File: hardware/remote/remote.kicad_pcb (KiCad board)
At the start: 2 copper layers, 106.7 x 86.4 mm, 25 parts

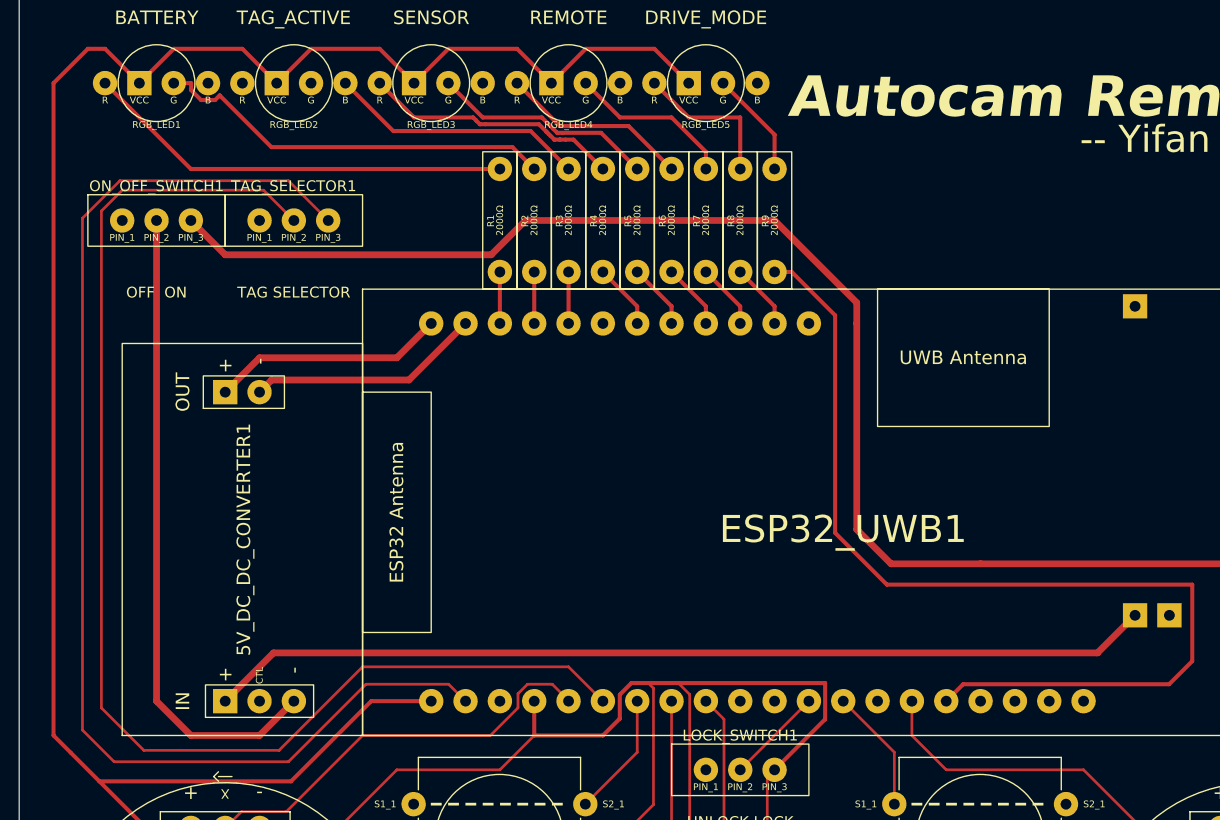
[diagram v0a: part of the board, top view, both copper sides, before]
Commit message: hardware/remote: Minor update to make more clearance for the antenna
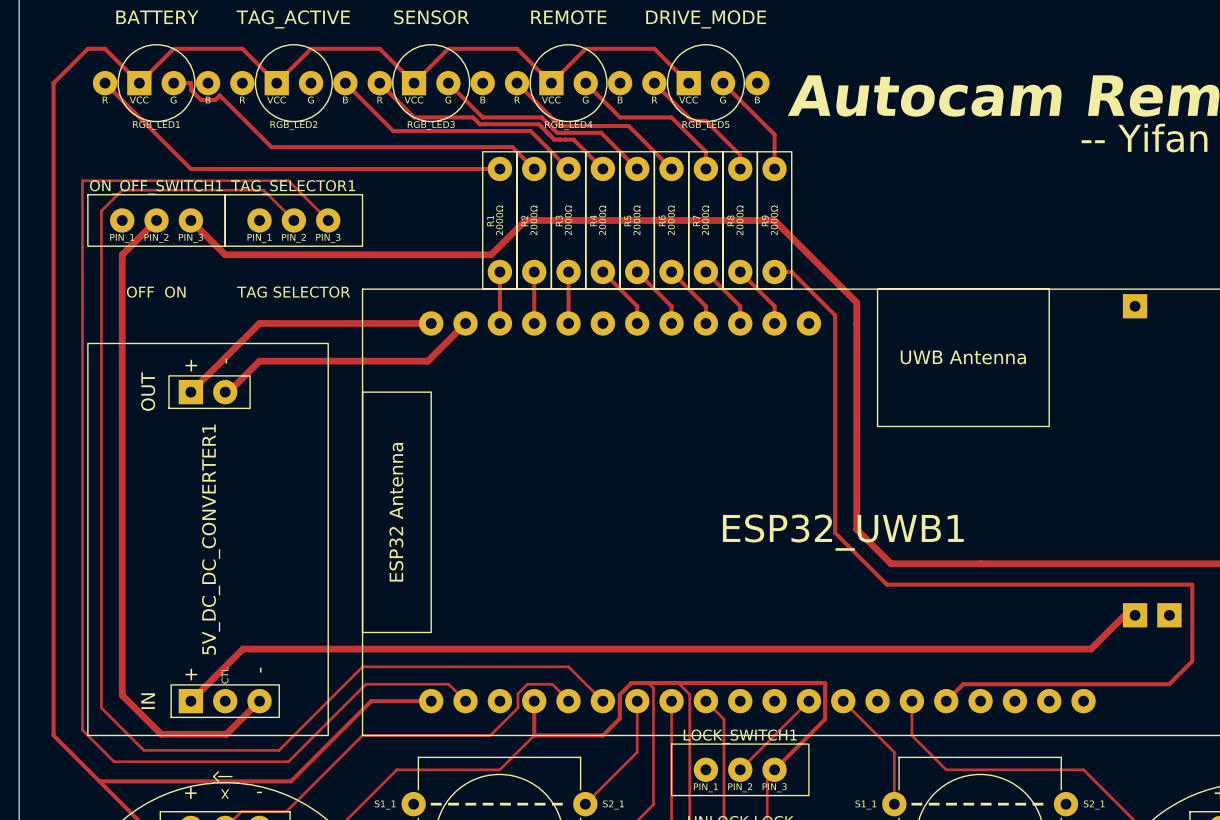
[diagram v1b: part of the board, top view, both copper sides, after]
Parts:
- moved 5V_DC_DC_CONVERTER1 2.54 mm to (99.1, 116.6)
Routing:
- net Net-(5V_DC_DC_CONVERTER1-OUT_-): track 17.3 -> 19.9 mm
- net Net-(5V_DC_DC_CONVERTER1-OUT_+): track 17.3 -> 19.9 mm
- net Net-(3.7V_BATTERY_CHARGER1-OUT+): track 69.9 -> 72.5 mm
- net Net-(RGB_LED5-R): track 11.2 -> 9.58 mm
- net Net-(ESP32_UWB1-GND-Pad2): track 90.6 -> 92.2 mm
- net Net-(5V_DC_DC_CONVERTER1-IN_-): track 47.8 -> 48.5 mm
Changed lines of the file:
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@@
 	(footprint "Autocam:5V DC-DC Step Up Converter (Rectangle)"
 		(layer "F.Cu")
-		(at 101.6 116.591058 90)
+		(at 99.06 116.591058 90)
 		(property "Reference" "5V_DC_DC_CONVERTER1"
 			(at 14.5 9 90)
@@
 	)
 	(segment
+		(start 110.531058 110.2)
+		(end 106.68 114.051058)
+		(width 0.5)
+		(layer "F.Cu")
+		(net 3)
+	)
+	(segment
 		(start 176.53 107.701058)
-		(end 173.750085 110.480973)
+		(end 175.769942 107.701058)
 		(width 0.5)
 		(layer "F.Cu")
@@
 	)
 	(segment
-		(start 112.790085 110.480973)
-		(end 109.22 114.051058)
+		(start 173.271 110.2)
+		(end 110.531058 110.2)
 		(width 0.5)
 		(layer "F.Cu")
@@
 	)
 	(segment
-		(start 173.750085 110.480973)
-		(end 112.790085 110.480973)
+		(start 175.769942 107.701058)
+		(end 173.271 110.2)
 		(width 0.5)
 		(layer "F.Cu")
@@
 	)
 	(segment
-		(start 112.66 90.291058)
-		(end 122.82 90.291058)
+		(start 124.211058 88.9)
+		(end 127 86.111058)
 		(width 0.5)
 		(layer "F.Cu")
@@
 	)
 	(segment
-		(start 122.82 90.291058)
-		(end 127 86.111058)
+		(start 109.468942 91.191058)
+		(end 111.76 88.9)
 		(width 0.5)
 		(layer "F.Cu")
@@
 	)
 	(segment
-		(start 111.76 91.191058)
-		(end 112.66 90.291058)
+		(start 109.22 91.191058)
+		(end 109.468942 91.191058)
 		(width 0.5)
 		(layer "F.Cu")
@@
 	)
 	(segment
-		(start 111.76 88.651058)
-		(end 121.92 88.651058)
+		(start 111.76 88.9)
+		(end 124.211058 88.9)
 		(width 0.5)
 		(layer "F.Cu")
-		(net 8)
+		(net 7)
 	)
 	(segment
-		(start 121.92 88.651058)
+		(start 111.76 86.111058)
 		(end 124.46 86.111058)
 		(width 0.5)
@@
 	)
 	(segment
-		(start 109.22 91.191058)
-		(end 111.76 88.651058)
+		(start 106.68 91.191058)
+		(end 111.76 86.111058)
 		(width 0.5)
 		(layer "F.Cu")
@@
 	)
 	(segment
-		(start 106.68 116.591058)
-		(end 111.76 116.591058)
+		(start 104.48 116.5)
+		(end 101.6 113.62)
 		(width 0.5)
 		(layer "F.Cu")
@@
 	)
 	(segment
-		(start 104.14 114.051058)
-		(end 106.68 116.591058)
+		(start 101.6 81.031058)
+		(end 104.14 78.491058)
 		(width 0.5)
 		(layer "F.Cu")
@@
 	)
 	(segment
-		(start 111.76 116.591058)
-		(end 114.3 114.051058)
+		(start 111.76 114.051058)
+		(end 109.311058 116.5)
 		(width 0.5)
 		(layer "F.Cu")
@@
 	)
 	(segment
-		(start 104.14 78.491058)
-		(end 104.14 114.051058)
+		(start 101.6 113.62)
+		(end 101.6 81.031058)
+		(width 0.5)
+		(layer "F.Cu")
+		(net 9)
+	)
+	(segment
+		(start 109.311058 116.5)
+		(end 104.48 116.5)
 		(width 0.5)
 		(layer "F.Cu")
@@
 	)
 	(segment
-		(start 119.631 112.800058)
-		(end 125.749 112.800058)
+		(start 98.659 116.190058)
+		(end 101.001 118.532058)
 		(width 0.2)
 		(layer "F.Cu")
@@
 	)
 	(segment
-		(start 98.659 116.190058)
-		(end 101.001 118.532058)
-		(width 0.2)
-		(layer "F.Cu")
-		(net 59)
-	)
-	(segment
-		(start 116.84 78.491058)
-		(end 113.899 75.550058)
+		(start 101.001 118.532058)
+		(end 113.899 118.532058)
 		(width 0.2)
 		(layer "F.Cu")
@@
 	)
 	(segment
-		(start 98.659 78.324958)
+		(start 98.659 75.550058)
 		(end 98.659 116.190058)
 		(width 0.2)
@@
 	)
 	(segment
-		(start 101.4339 75.550058)
-		(end 98.659 78.324958)
+		(start 113.899 75.550058)
+		(end 98.659 75.550058)
 		(width 0.2)
 		(layer "F.Cu")
@@
 	)
 	(segment
-		(start 113.899 75.550058)
-		(end 101.4339 75.550058)
+		(start 119.631 112.800058)
+		(end 125.749 112.800058)
 		(width 0.2)
 		(layer "F.Cu")
@@
 	)
 	(segment
-		(start 101.001 118.532058)
-		(end 113.899 118.532058)
+		(start 116.84 78.491058)
+		(end 113.899 75.550058)
 		(width 0.2)
 		(layer "F.Cu")
@@
 	)
 	(segment
-		(start 147.32 70.871058)
-		(end 147.32 74.681058)
+		(start 144.78 71.12)
+		(end 143.758942 71.12)
+		(width 0.3)
+		(layer "F.Cu")
+		(net 71)
+	)
+	(segment
+		(start 147.32 73.66)
+		(end 144.78 71.12)
 		(width 0.3)
 		(layer "F.Cu")
@@
 	)
 	(segment
-		(start 143.51 70.871058)
-		(end 147.32 70.871058)
+		(start 143.758942 71.12)
+		(end 140.97 68.331058)
 		(width 0.3)
 		(layer "F.Cu")
@@
 	)
 	(segment
-		(start 140.97 68.331058)
-		(end 143.51 70.871058)
+		(start 147.32 74.681058)
+		(end 147.32 73.66)
 		(width 0.3)
 		(layer "F.Cu")

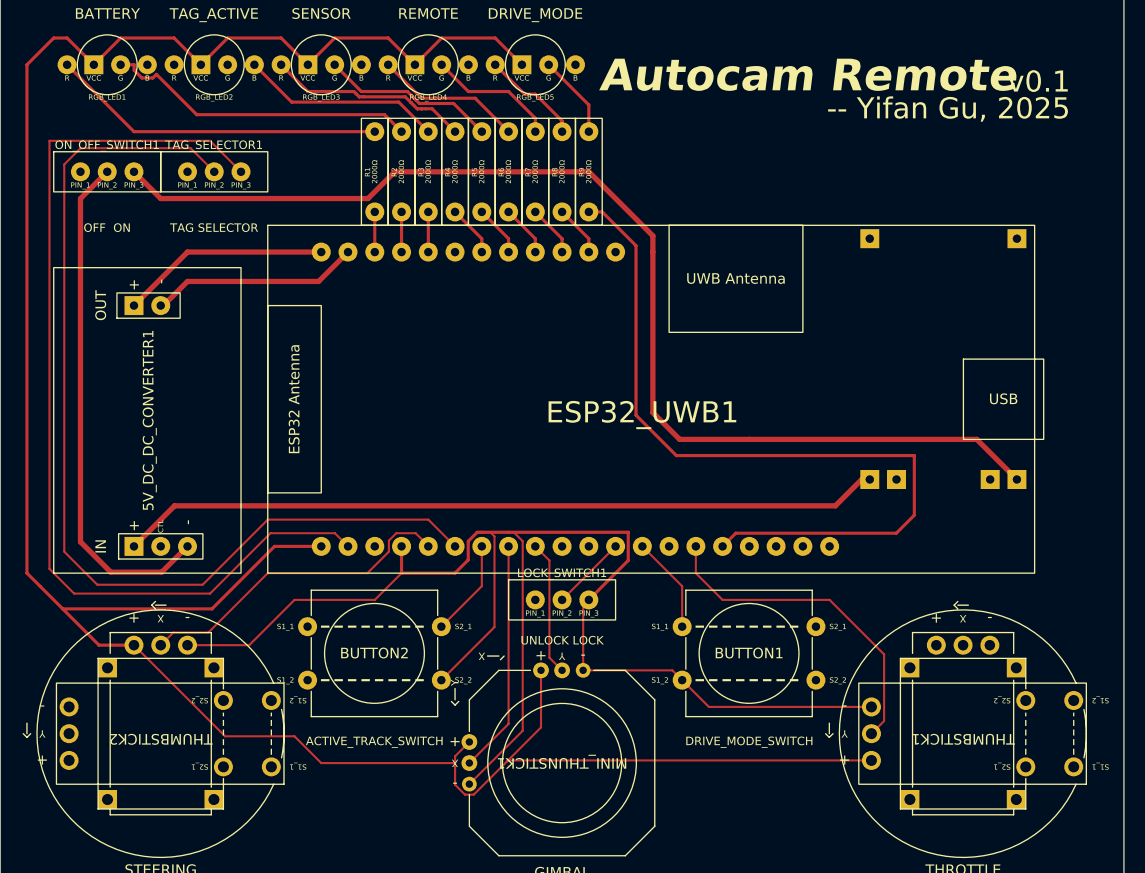
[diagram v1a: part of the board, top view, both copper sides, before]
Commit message: remote: Add battery status LED logic.
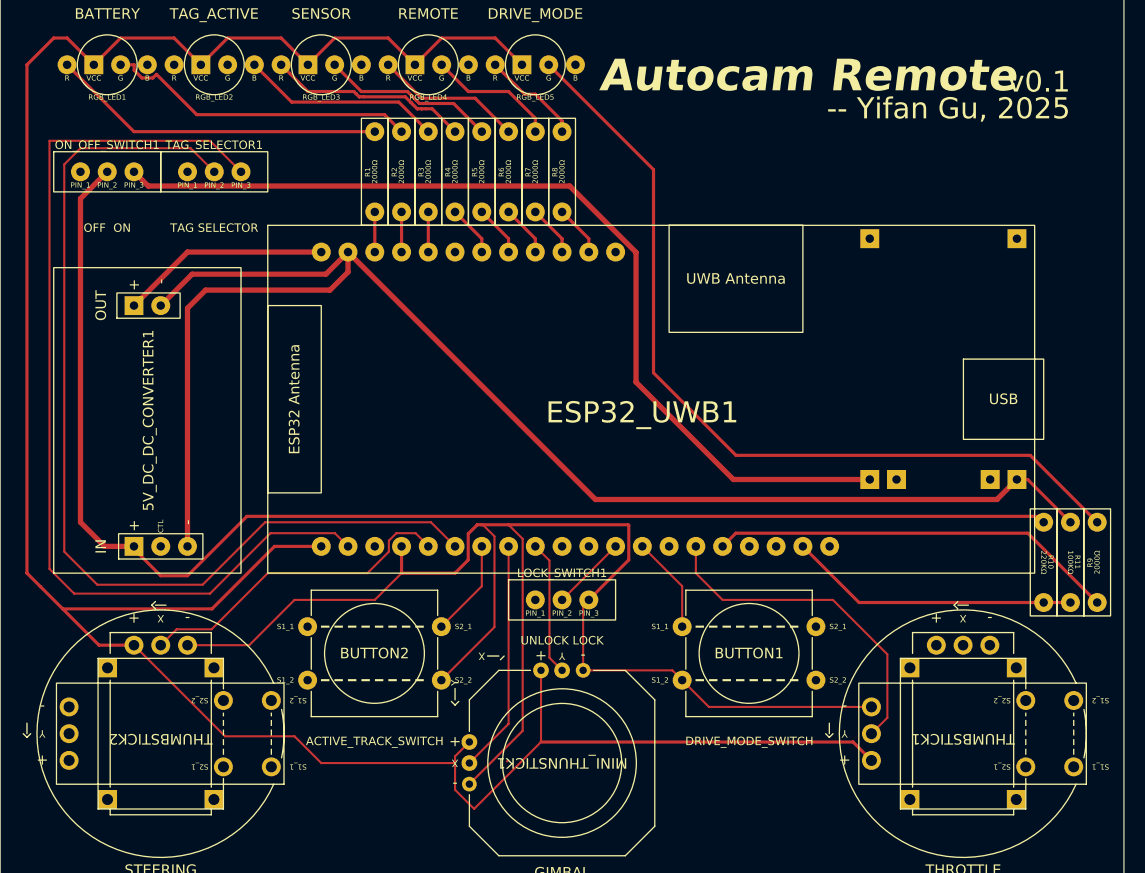
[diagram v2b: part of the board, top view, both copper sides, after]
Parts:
- added R10: 220KΩ, Autocam:Simple Resistor, F.Cu at (193.0, 111.8)
- added R11: 100KΩ, Autocam:Simple Resistor, F.Cu at (195.6, 111.8)
- moved R9 60.9 mm to (198.1, 119.4)
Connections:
- 5V_DC_DC_CONVERTER1 pad 1: Net-(3.7V_BATTERY_CHARGER1-OUT+) -> Net-(5V_DC_DC_CONVERTER1-IN_+)
- 5V_DC_DC_CONVERTER1 pad 3: Net-(5V_DC_DC_CONVERTER1-IN_-) -> Net-(3.7V_BATTERY_CHARGER1-OUT-)
- 5V_DC_DC_CONVERTER1 pad 5: Net-(5V_DC_DC_CONVERTER1-OUT_-) -> Net-(3.7V_BATTERY_CHARGER1-OUT-)
- ESP32_UWB1 pad 19: unconnected-(ESP32_UWB1-IO36-Pad19) -> Net-(ESP32_UWB1-IO36)
- ESP32_UWB1 pad 22: Net-(5V_DC_DC_CONVERTER1-OUT_-) -> Net-(3.7V_BATTERY_CHARGER1-OUT-)
- ON_OFF_SWITCH1 pad 2: Net-(5V_DC_DC_CONVERTER1-IN_-) -> Net-(5V_DC_DC_CONVERTER1-IN_+)
- ON_OFF_SWITCH1 pad 3: Net-(3.7V_BATTERY_CHARGER1-OUT-) -> Net-(3.7V_BATTERY_CHARGER1-OUT+)
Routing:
- net Net-(5V_DC_DC_CONVERTER1-IN_+): track 0.00 -> 129.8 mm
- net Net-(RGB_LED5-G): track 7.93 -> 81.4 mm
- net Net-(5V_DC_DC_CONVERTER1-IN_-): track 48.5 -> 0.00 mm
- net Net-(ESP32_UWB1-IO33): track 75.0 -> 38.8 mm
- net Net-(3.7V_BATTERY_CHARGER1-OUT-): track 107.9 -> 142.1 mm
- net Net-(ESP32_UWB1-IO36): track 0.00 -> 27.6 mm
- net Net-(5V_DC_DC_CONVERTER1-OUT_-): track 19.9 -> 0.00 mm
- net Net-(3.7V_BATTERY_CHARGER1-OUT+): track 72.5 -> 89.4 mm
- net Net-(BUTTON1-S1_2): track 137.5 -> 139.7 mm

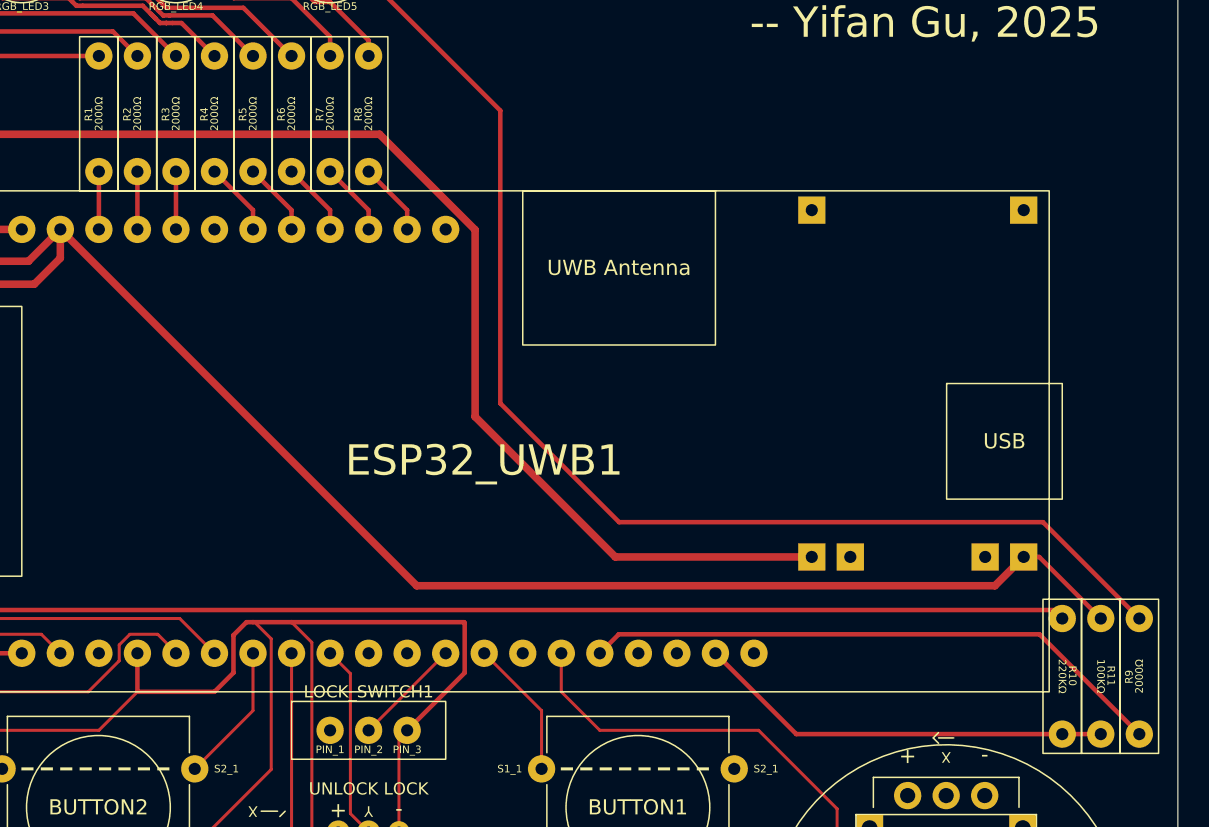
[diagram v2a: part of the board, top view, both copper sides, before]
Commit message: hardware: Increase the LED resistor from 2000Ω to 10KΩ.
To reduce the power consumption.
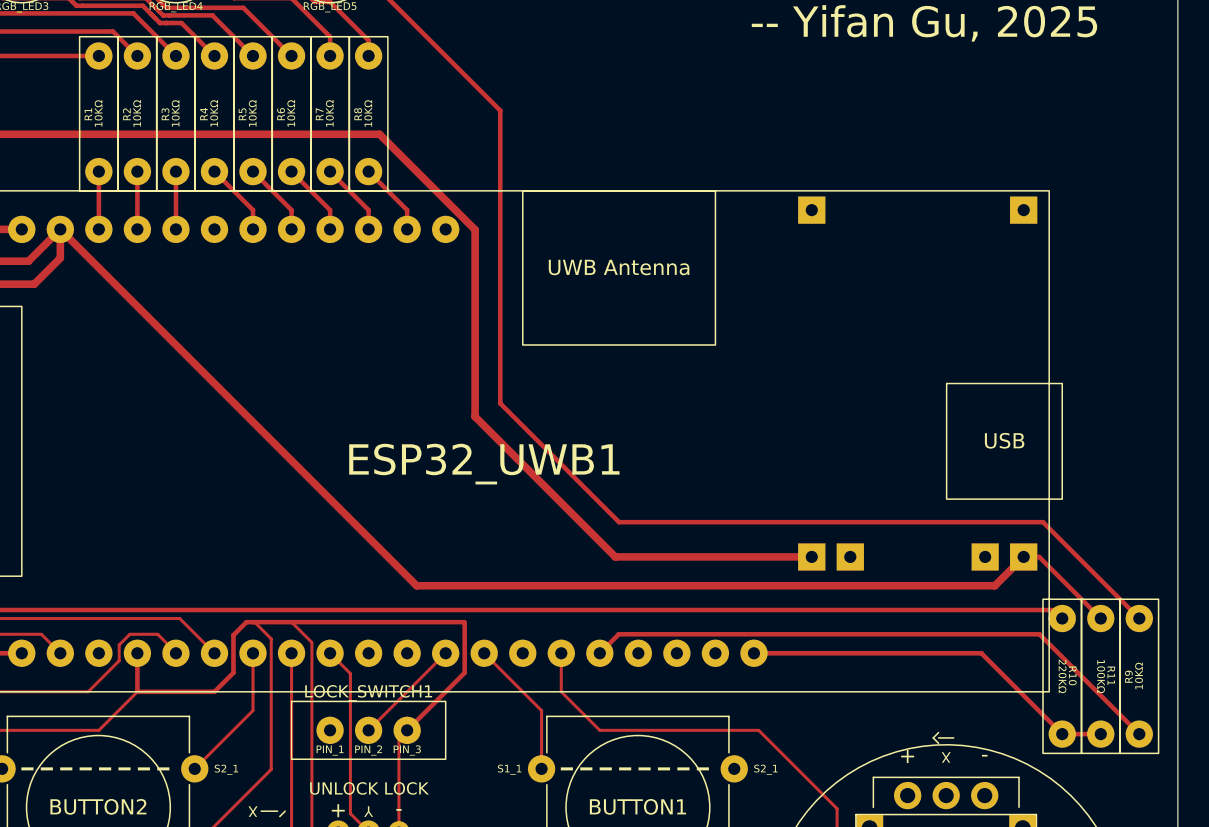
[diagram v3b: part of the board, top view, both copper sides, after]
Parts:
- R1, R2, R3, R4, R5, R6, R7, R8, R9: value 2000Ω -> 10KΩ
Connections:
- ESP32_UWB1 pad 19: Net-(ESP32_UWB1-IO36) -> unconnected-(ESP32_UWB1-IO36-Pad19)
- ESP32_UWB1 pad 20: unconnected-(ESP32_UWB1-IO39-Pad20) -> Net-(ESP32_UWB1-IO39)
- R10 pad 2: Net-(ESP32_UWB1-IO36) -> Net-(ESP32_UWB1-IO39)
- R11 pad 2: Net-(ESP32_UWB1-IO36) -> Net-(ESP32_UWB1-IO39)
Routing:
- net Net-(ESP32_UWB1-IO36): track 27.6 -> 0.00 mm
- net Net-(ESP32_UWB1-IO39): track 0.00 -> 25.1 mm
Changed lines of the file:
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@@
 	(net 14 "unconnected-(BUTTON2-S1_2-Pad2)")
 	(net 15 "unconnected-(ESP32_UWB1-IO35-Pad18)")
-	(net 16 "unconnected-(ESP32_UWB1-IO39-Pad20)")
+	(net 16 "unconnected-(ESP32_UWB1-IO36-Pad19)")
 	(net 17 "Net-(ESP32_UWB1-3V3)")
 	(net 18 "unconnected-(ESP32_UWB1-IO34-Pad17)")
-	(net 19 "Net-(ESP32_UWB1-IO36)")
+	(net 19 "Net-(ESP32_UWB1-IO39)")
 	(net 20 "unconnected-(ESP32_UWB1-RST-Pad3)")
 	(net 21 "unconnected-(BUTTON2-S1_1-Pad1)")
@@
 			)
 		)
-		(property "Value" "2000Ω"
+		(property "Value" "10KΩ"
 			(at 3.81 0 90)
 			(unlocked yes)
@@
 			)
 		)
-		(property "Value" "2000Ω"
+		(property "Value" "10KΩ"
 			(at 3.81 0 90)
 			(unlocked yes)
@@
 			)
 		)
-		(property "Value" "2000Ω"
+		(property "Value" "10KΩ"
 			(at 3.81 0 90)
 			(unlocked yes)
@@
 			(layers "*.Cu" "*.Mask")
 			(remove_unused_layers no)
-			(net 19 "Net-(ESP32_UWB1-IO36)")
+			(net 19 "Net-(ESP32_UWB1-IO39)")
 			(pintype "passive")
 		)
@@
 			(layers "*.Cu" "*.Mask")
 			(remove_unused_layers no)
-			(net 19 "Net-(ESP32_UWB1-IO36)")
+			(net 16 "unconnected-(ESP32_UWB1-IO36-Pad19)")
 			(pinfunction "IO36")
 			(pintype "bidirectional")
@@
 			(layers "*.Cu" "*.Mask")
 			(remove_unused_layers no)
-			(net 16 "unconnected-(ESP32_UWB1-IO39-Pad20)")
+			(net 19 "Net-(ESP32_UWB1-IO39)")
 			(pinfunction "IO39")
 			(pintype "bidirectional")
@@
 			)
 		)
-		(property "Value" "2000Ω"
+		(property "Value" "10KΩ"
 			(at 3.81 0 90)
 			(unlocked yes)
@@
 			)
 		)
-		(property "Value" "2000Ω"
+		(property "Value" "10KΩ"
 			(at 3.81 0 90)
 			(unlocked yes)
@@
 			)
 		)
-		(property "Value" "2000Ω"
+		(property "Value" "10KΩ"
 			(at 3.81 0 90)
 			(unlocked yes)
@@
 			)
 		)
-		(property "Value" "2000Ω"
+		(property "Value" "10KΩ"
 			(at 3.81 0 90)
 			(unlocked yes)
@@
 			(layers "*.Cu" "*.Mask")
 			(remove_unused_layers no)
-			(net 19 "Net-(ESP32_UWB1-IO36)")
+			(net 19 "Net-(ESP32_UWB1-IO39)")
 			(pintype "passive")
 		)
@@
 			)
 		)
-		(property "Value" "2000Ω"
+		(property "Value" "10KΩ"
 			(at 3.81 0 90)
 			(unlocked yes)
@@
 			)
 		)
-		(property "Value" "2000Ω"
+		(property "Value" "10KΩ"
 			(at 3.81 0 90)
 			(unlocked yes)
@@
 	)
 	(segment
-		(start 175.508942 119.38)
-		(end 170.18 114.051058)
+		(start 172.72 114.051058)
+		(end 187.711058 114.051058)
 		(width 0.3)
 		(layer "F.Cu")
@@
 	)
 	(segment
-		(start 193.04 119.38)
-		(end 175.508942 119.38)
+		(start 187.711058 114.051058)
+		(end 193.04 119.38)
 		(width 0.3)
 		(layer "F.Cu")
